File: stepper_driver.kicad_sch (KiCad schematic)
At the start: 32 parts, among them SW1 SW_DIP_x04, SW2 SW_DIP_x04, U1 TMC2160A-TA-T

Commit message: Added symbol library
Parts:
- R10: value (none) -> 2.2R; footprint (none) -> Resistor_SMD:R_0805_2012Metric
- U1: value TMC2160A-TA-T -> (none); footprint Package_QFP:TQFP-48-1EP_7x7mm_P0.5mm_EP5x5mm_ThermalVias -> (none)
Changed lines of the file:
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@@
     (in_bom yes) (on_board yes)
     (property "Reference" "U1" (id 0) (at 81.28 135.89 0))
-    (property "Value" "TMC2160A-TA-T" (id 1) (at 80.01 133.35 0))
-    (property "Footprint" "Package_QFP:TQFP-48-1EP_7x7mm_P0.5mm_EP5x5mm_ThermalVias" (id 2) (at 68.58 147.32 0)
+    (property "Value" "" (id 1) (at 80.01 133.35 0))
+    (property "Footprint" "" (id 2) (at 68.58 147.32 0)
       (effects (font (size 1.27 1.27)) hide)
     )
@@
     (in_bom yes) (on_board yes)
     (property "Reference" "R10" (id 0) (at 46.99 16.51 90))
-    (property "Value" "" (id 1) (at 46.99 19.05 90))
-    (property "Footprint" "" (id 2) (at 46.99 23.368 90)
+    (property "Value" "2.2R" (id 1) (at 46.99 19.05 90))
+    (property "Footprint" "Resistor_SMD:R_0805_2012Metric" (id 2) (at 46.99 23.368 90)
       (effects (font (size 1.27 1.27)) hide)
     )

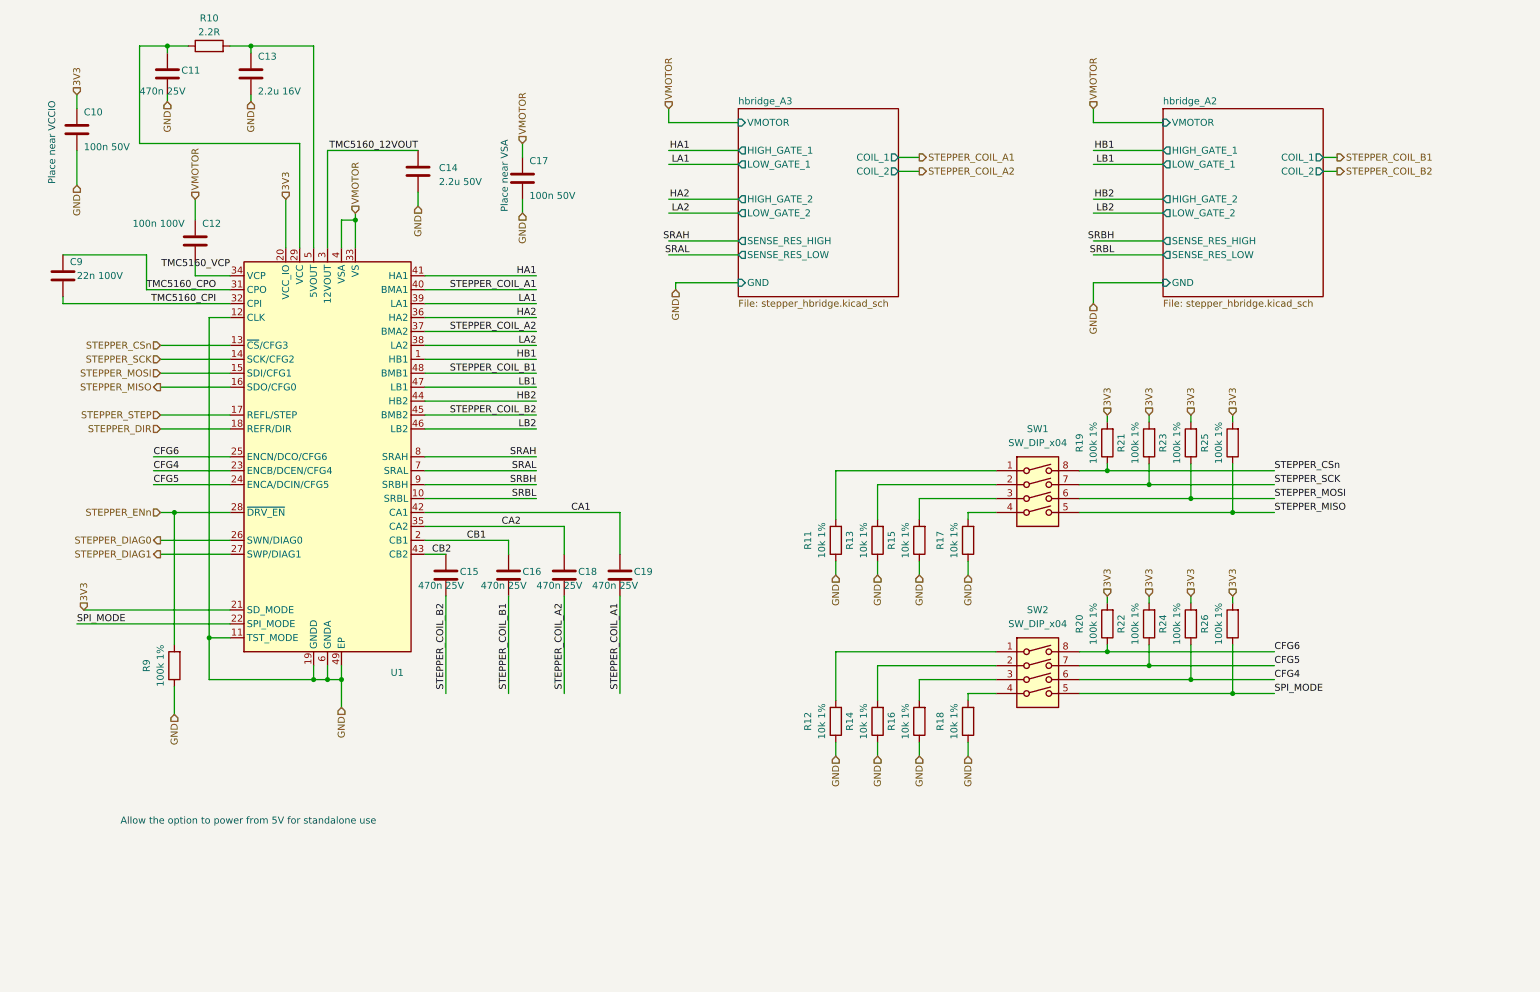
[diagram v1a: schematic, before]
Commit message: Removed caps from board. Will be placed on main board
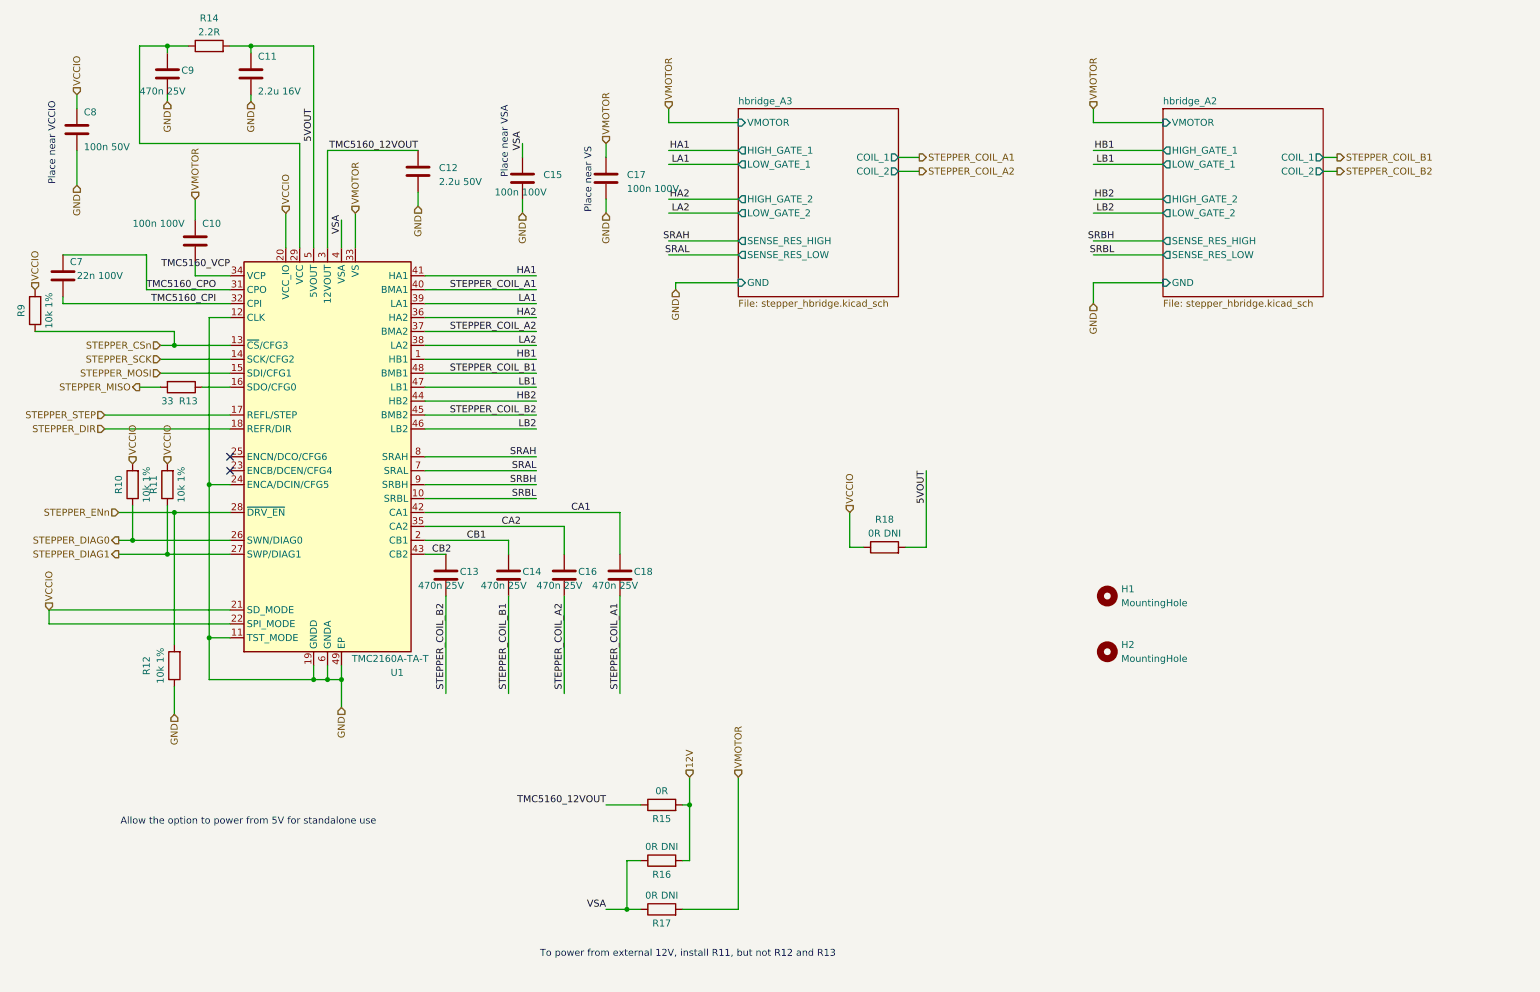
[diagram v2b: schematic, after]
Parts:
- removed R12, R14: 10k 1%, Resistor_SMD:R_0402_1005Metric, symbol Device:R
- removed R19, R20, R21, R22, R23, R24, R25, R26: 100k 1%, Resistor_SMD:R_0402_1005Metric, symbol Device:R
- removed SW1, SW2: SW_DIP_x04, Button_Switch_SMD:SW_DIP_SPSTx04_Slide_Omron_A6H-4101_W6.15mm_P1.27mm, symbol Switch:SW_DIP_x04
- added C15: 100n 100V, Capacitor_SMD:C_0805_2012Metric_Pad1.18x1.45mm_HandSolder, symbol Device:C
- added H1, H2: MountingHole, MountingHole:MountingHole_3.2mm_M3, symbol Mechanical:MountingHole
- added R10, R9: 10k 1%, Resistor_SMD:R_0402_1005Metric, symbol Device:R
- C12: renamed from C14; footprint Capacitor_SMD:C_1206_3216Metric -> Capacitor_SMD:C_0805_2012Metric; LCSC C50254 -> C49217
- C17: value 100n 50V -> 100n 100V; footprint Capacitor_SMD:C_0402_1005Metric -> Capacitor_SMD:C_0805_2012Metric_Pad1.18x1.45mm_HandSolder; LCSC C307331 -> C28233
- C7: renamed from C9; footprint Capacitor_SMD:C_0805_2012Metric -> Capacitor_SMD:C_0402_1005Metric; LCSC C107137 -> C1532
- R12: renamed from R9; value 100k 1% -> 10k 1%; LCSC C25741 -> C25744
- R13: value 10k 1% -> 33; LCSC C25744 -> C25105
- R14: renamed from R10; footprint Resistor_SMD:R_0805_2012Metric -> Resistor_SMD:R_0603_1608Metric; LCSC C17521 -> C22939
- R15: value 10k 1% -> 0R; LCSC C25744 -> C17168
- R16, R17: value 10k 1% -> 0R DNI; LCSC C25744 -> (none)
- R18: value 10k 1% -> 0R DNI; footprint Resistor_SMD:R_0402_1005Metric -> Resistor_SMD:R_0805_2012Metric; LCSC C25744 -> (none)
- U1: value (none) -> TMC2160A-TA-T; footprint (none) -> Package_QFP:TQFP-48-1EP_7x7mm_P0.5mm_EP5x5mm_ThermalVias
- renumbered C12 to C10, C13 to C11, C15 to C13, C16 to C14, C18 to C16, C19 to C18, C10 to C8, C11 to C9
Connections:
- net 3V3 is gone; now on net VCCIO: C8.1, U1.20 (VCC_IO), U1.21 (SD_MODE)
- net CFG5 is gone; now on net GND: U1.24 (ENCA/DCIN/CFG5)
- net SPI_MODE is gone; now on net VCCIO: U1.22 (SPI_MODE)
- net GND: now also C15.2; no longer R11.1, R13.1, R15.1, R16.1, R17.1, R18.1
- net STEPPER_CSn: now also R9.1
- net STEPPER_DIAG0: now also R10.1
- net STEPPER_DIAG1: now also R11.1
- net STEPPER_MISO: now also R13.2; no longer U1.16 (SDO/CFG0)
- net TMC5160_12VOUT: now also R15.1
- net VMOTOR: now also R17.2; no longer U1.4 (VSA)
- net 5VOUT: now reaches R18.2
- net 5VOUT: now also C11.1, R14.2, U1.5 (5VOUT)
- net 12V: now reaches R16.2
- net 12V: now also R15.2
- net VCCIO: now reaches R11.2
- net VCCIO: now also R18.1, R10.2, R9.2
- net CFG4: no longer names the net of U1.23 (ENCB/DCEN/CFG4)
- net CFG6: no longer names the net of U1.25 (ENCN/DCO/CFG6)
- new net: R13.1, U1.16 (SDO/CFG0)
- new net VSA: C15.1, R16.1, R17.1, U1.4 (VSA)
- no-connect marks 0 -> 2
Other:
- note added: "Place near VS"
- note added: "To power from external 12V, install R11, but not R12 and R13"

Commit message: Removed 0Ohms. Keyed design
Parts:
- removed R11: 10k 1%, Resistor_SMD:R_0402_1005Metric, symbol Device:R
- removed R15: 0R, Resistor_SMD:R_0402_1005Metric, symbol Device:R
- removed R16, R17: 0R DNI, Resistor_SMD:R_0402_1005Metric, symbol Device:R
- removed R18: 0R DNI, Resistor_SMD:R_0805_2012Metric, symbol Device:R
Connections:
- net TMC5160_12VOUT is gone; now on net 12V: C12.1, U1.3 (12VOUT)
- net STEPPER_DIAG1: no longer names the net of U1.27 (SWP/DIAG1)
- no-connect marks 2 -> 3

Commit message: Updated pinout
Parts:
- added R8: 10k 1%, Resistor_SMD:R_0402_1005Metric, symbol Device:R
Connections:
- net VCCIO: now also R8.2
- net STEPPER_DIAG1: now reaches U1.27 (SWP/DIAG1)
- net STEPPER_DIAG1: now also R8.1
- no-connect marks 3 -> 2
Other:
- moved on the sheet: C10, C11, C12, C13, C14, C15, C16, C17, C18, C7, C8, C9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
